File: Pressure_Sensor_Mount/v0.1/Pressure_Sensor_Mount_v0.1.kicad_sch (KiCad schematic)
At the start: 2 parts, among them J1 Conn_01x04_Pin

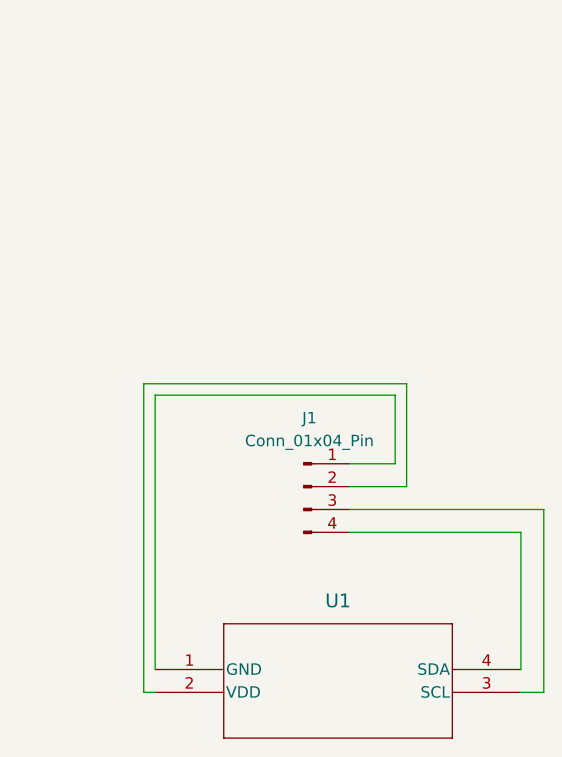
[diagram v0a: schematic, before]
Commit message: Full Rework of NanoBoard Libraries, Updated Final Version of NB101
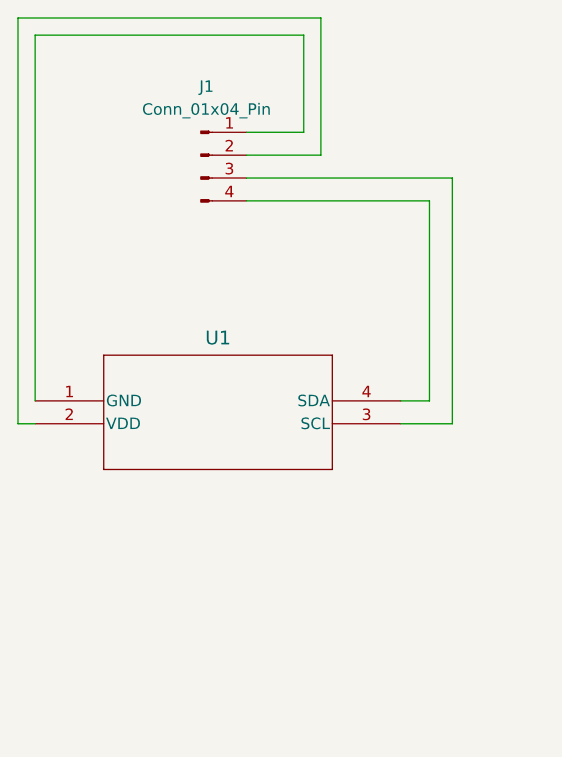
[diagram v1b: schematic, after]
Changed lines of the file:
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@@
 (kicad_sch (version 20230121) (generator eeschema)
   (paper "A4")
-  (wire (pts (xy 140.97 92.71) (xy 160.02 92.71))
+  (wire (pts (xy 137.795 35.56) (xy 137.795 50.8))
     (stroke (width 0) (type default))
   )
-  (wire (pts (xy 162.56 110.49) (xy 160.02 110.49))
+  (wire (pts (xy 106.045 78.105) (xy 106.045 37.465))
     (stroke (width 0) (type default))
   )
-  (wire (pts (xy 147.32 76.2) (xy 147.32 87.63))
+  (wire (pts (xy 104.14 35.56) (xy 137.795 35.56))
     (stroke (width 0) (type default))
   )
-  (wire (pts (xy 147.32 87.63) (xy 140.97 87.63))
+  (wire (pts (xy 152.4 80.645) (xy 146.685 80.645))
     (stroke (width 0) (type default))
   )
-  (wire (pts (xy 160.02 107.95) (xy 160.02 92.71))
+  (wire (pts (xy 152.4 53.34) (xy 152.4 80.645))
     (stroke (width 0) (type default))
   )
-  (wire (pts (xy 140.97 90.17) (xy 162.56 90.17))
+  (wire (pts (xy 129.54 53.34) (xy 152.4 53.34))
     (stroke (width 0) (type default))
   )
-  (wire (pts (xy 162.56 90.17) (xy 162.56 110.49))
+  (wire (pts (xy 106.045 37.465) (xy 135.89 37.465))
     (stroke (width 0) (type default))
   )
-  (wire (pts (xy 119.38 107.95) (xy 119.38 77.47))
+  (wire (pts (xy 129.54 55.88) (xy 149.86 55.88))
     (stroke (width 0) (type default))
   )
-  (wire (pts (xy 146.05 77.47) (xy 146.05 85.09))
+  (wire (pts (xy 137.795 50.8) (xy 129.54 50.8))
     (stroke (width 0) (type default))
   )
-  (wire (pts (xy 119.38 110.49) (xy 118.11 110.49))
+  (wire (pts (xy 106.045 80.645) (xy 104.14 80.645))
     (stroke (width 0) (type default))
   )
-  (wire (pts (xy 118.11 76.2) (xy 147.32 76.2))
+  (wire (pts (xy 135.89 48.26) (xy 129.54 48.26))
     (stroke (width 0) (type default))
   )
-  (wire (pts (xy 119.38 77.47) (xy 146.05 77.47))
+  (wire (pts (xy 135.89 37.465) (xy 135.89 48.26))
     (stroke (width 0) (type default))
   )
-  (wire (pts (xy 118.11 110.49) (xy 118.11 76.2))
+  (wire (pts (xy 149.86 78.105) (xy 146.685 78.105))
     (stroke (width 0) (type default))
   )
-  (wire (pts (xy 146.05 85.09) (xy 140.97 85.09))
+  (wire (pts (xy 104.14 80.645) (xy 104.14 35.56))
     (stroke (width 0) (type default))
   )
-  (symbol (lib_id "MS583730BA01-50 (NanoFloat Pressure Sensor):MS583730BA01-50") (at 119.38 107.95 0) (unit 1)
+  (wire (pts (xy 149.86 55.88) (xy 149.86 78.105))
+    (stroke (width 0) (type default))
+  )
+  (symbol (lib_id "MS583730BA01-50 (NanoFloat Pressure Sensor):MS583730BA01-50") (at 106.045 78.105 0) (unit 1)
     (in_bom yes) (on_board yes) (dnp no) (fields_autoplaced)
-    (property "Reference" "U1" (at 139.7 100.33 0)
+    (property "Reference" "U1" (at 126.365 71.12 0)
       (effects (font (size 1.524 1.524)))
     )
-    (property "Value" "~" (at 139.7 100.33 0)
+    (property "Value" "~" (at 126.365 70.485 0)
       (effects (font (size 1.524 1.524)))
     )
-    (property "Footprint" "NanoFloat Pressure Sensor:Pressure Sensor Footprint" (at 139.7 114.3 0)
+    (property "Footprint" "NanoFloat Pressure Sensor:Pressure Sensor Footprint" (at 126.365 84.455 0)
       (effects (font (size 1.27 1.27) italic) hide)
     )
-    (property "Datasheet" "MS583730BA01-50" (at 139.7 105.41 0)
+    (property "Datasheet" "MS583730BA01-50" (at 126.365 75.565 0)
       (effects (font (size 1.27 1.27) italic) hide)
     )
+    (pin "4")
+    (pin "3")
     (pin "1")
-    (pin "3")
     (pin "2")
-    (pin "4")
     (instances
-      (project "nanofloat-pressure-sensor-mount"
+      (project "Pressure_Sensor_Mount_v0.1"
         (path "/36745fa6-eaa2-467e-b9f0-5e9a6d81871a"
           (reference "U1") (unit 1)
@@
     )
   )
-  (symbol (lib_id "Connector:Conn_01x04_Pin") (at 135.89 87.63 0) (unit 1)
+  (symbol (lib_id "Connector:Conn_01x04_Pin") (at 124.46 50.8 0) (unit 1)
     (in_bom yes) (on_board yes) (dnp no) (fields_autoplaced)
-    (property "Reference" "J1" (at 136.525 80.01 0)
+    (property "Reference" "J1" (at 125.095 43.18 0)
       (effects (font (size 1.27 1.27)))
     )
-    (property "Value" "Conn_01x04_Pin" (at 136.525 82.55 0)
+    (property "Value" "Conn_01x04_Pin" (at 125.095 45.72 0)
       (effects (font (size 1.27 1.27)))
     )
-    (property "Footprint" "Connector_PinHeader_2.54mm:PinHeader_1x04_P2.54mm_Vertical" (at 135.89 87.63 0)
+    (property "Footprint" "Connector_PinHeader_2.54mm:PinHeader_1x04_P2.54mm_Vertical" (at 124.46 50.8 0)
       (effects (font (size 1.27 1.27)) hide)
     )
-    (property "Datasheet" "~" (at 135.89 87.63 0)
+    (property "Datasheet" "~" (at 124.46 50.8 0)
       (effects (font (size 1.27 1.27)) hide)
     )
-    (pin "4")
     (pin "3")
     (pin "1")
+    (pin "4")
     (pin "2")
     (instances
-      (project "nanofloat-pressure-sensor-mount"
+      (project "Pressure_Sensor_Mount_v0.1"
         (path "/36745fa6-eaa2-467e-b9f0-5e9a6d81871a"
           (reference "J1") (unit 1)
